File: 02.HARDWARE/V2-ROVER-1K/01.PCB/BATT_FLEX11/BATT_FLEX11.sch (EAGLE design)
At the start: 4 parts, among them K3 FLEX11, K4 FLEX11, K7 FLEX11, K8 FLEX11

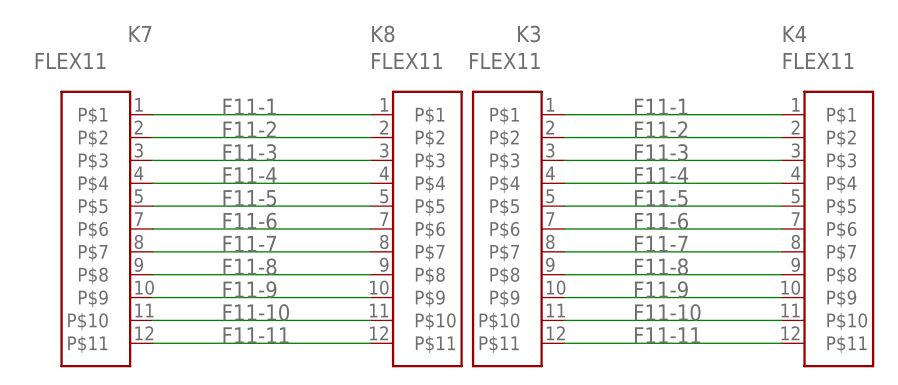
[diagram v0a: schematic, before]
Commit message: Ajuste de ancho de pista para lineas de potencias.
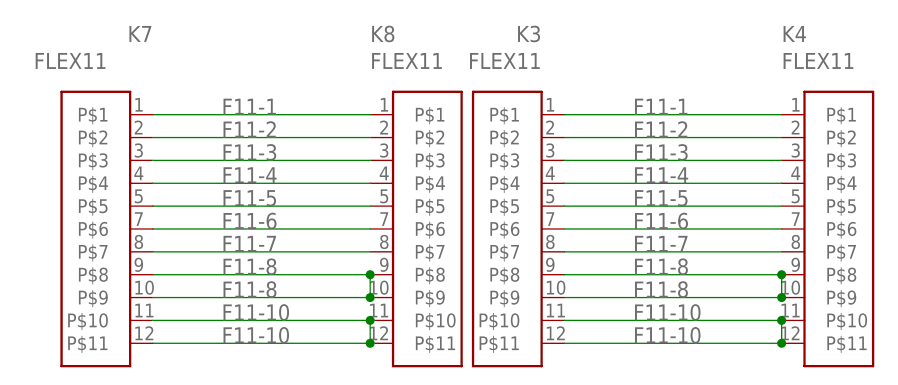
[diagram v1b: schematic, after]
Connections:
- removed net F11-11: K3.P$11, K4.P$11, K7.P$11, K8.P$11
- removed net F11-9: K3.P$9, K4.P$9, K7.P$9, K8.P$9
- net F11-10: now also K3.P$11, K4.P$11, K7.P$11, K8.P$11
- net F11-8: now also K3.P$9, K4.P$9, K7.P$9, K8.P$9
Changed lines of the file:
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@@
 <wire x1="124.46" y1="76.2" x2="148.59" y2="76.2" width="0.1524" layer="91"/>
 <label x="132.08" y="76.2" size="1.778" layer="95"/>
+<pinref part="K3" gate="G$1" pin="P$9"/>
+<pinref part="K4" gate="G$1" pin="P$9"/>
+<wire x1="124.46" y1="73.66" x2="148.59" y2="73.66" width="0.1524" layer="91"/>
+<label x="132.08" y="73.66" size="1.778" layer="95"/>
+<wire x1="148.59" y1="76.2" x2="148.59" y2="73.66" width="0.1524" layer="91"/>
+<junction x="148.59" y="76.2"/>
+<junction x="148.59" y="73.66"/>
 </segment>
 <segment>
@@
 <wire x1="78.74" y1="76.2" x2="102.87" y2="76.2" width="0.1524" layer="91"/>
 <label x="86.36" y="76.2" size="1.778" layer="95"/>
+<pinref part="K7" gate="G$1" pin="P$9"/>
+<pinref part="K8" gate="G$1" pin="P$9"/>
+<wire x1="78.74" y1="73.66" x2="102.87" y2="73.66" width="0.1524" layer="91"/>
+<label x="86.36" y="73.66" size="1.778" layer="95"/>
+<wire x1="102.87" y1="76.2" x2="102.87" y2="73.66" width="0.1524" layer="91"/>
+<junction x="102.87" y="76.2"/>
+<junction x="102.87" y="73.66"/>
 </segment>
 </net>
@@
 </segment>
 </net>
-<net name="F11-9" class="0">
-<segment>
-<pinref part="K7" gate="G$1" pin="P$9"/>
-<pinref part="K8" gate="G$1" pin="P$9"/>
-<wire x1="78.74" y1="73.66" x2="102.87" y2="73.66" width="0.1524" layer="91"/>
-<label x="86.36" y="73.66" size="1.778" layer="95"/>
-</segment>
-<segment>
-<pinref part="K3" gate="G$1" pin="P$9"/>
-<pinref part="K4" gate="G$1" pin="P$9"/>
-<wire x1="124.46" y1="73.66" x2="148.59" y2="73.66" width="0.1524" layer="91"/>
-<label x="132.08" y="73.66" size="1.778" layer="95"/>
-</segment>
-</net>
 <net name="F11-10" class="0">
 <segment>
@@
 <pinref part="K8" gate="G$1" pin="P$10"/>
 <label x="86.36" y="71.12" size="1.778" layer="95"/>
+<pinref part="K7" gate="G$1" pin="P$11"/>
+<pinref part="K8" gate="G$1" pin="P$11"/>
+<wire x1="78.74" y1="68.58" x2="102.87" y2="68.58" width="0.1524" layer="91"/>
+<label x="86.36" y="68.58" size="1.778" layer="95"/>
+<wire x1="102.87" y1="71.12" x2="102.87" y2="68.58" width="0.1524" layer="91"/>
+<junction x="102.87" y="71.12"/>
+<junction x="102.87" y="68.58"/>
 </segment>
 <segment>
@@
 <wire x1="148.59" y1="71.12" x2="124.46" y2="71.12" width="0.1524" layer="91"/>
 <label x="132.08" y="71.12" size="1.778" layer="95"/>
-</segment>
-</net>
-<net name="F11-11" class="0">
-<segment>
-<pinref part="K7" gate="G$1" pin="P$11"/>
-<pinref part="K8" gate="G$1" pin="P$11"/>
-<wire x1="78.74" y1="68.58" x2="102.87" y2="68.58" width="0.1524" layer="91"/>
-<label x="86.36" y="68.58" size="1.778" layer="95"/>
-</segment>
-<segment>
 <pinref part="K3" gate="G$1" pin="P$11"/>
 <pinref part="K4" gate="G$1" pin="P$11"/>
 <wire x1="124.46" y1="68.58" x2="148.59" y2="68.58" width="0.1524" layer="91"/>
 <label x="132.08" y="68.58" size="1.778" layer="95"/>
+<wire x1="148.59" y1="71.12" x2="148.59" y2="68.58" width="0.1524" layer="91"/>
+<junction x="148.59" y="71.12"/>
+<junction x="148.59" y="68.58"/>
 </segment>
 </net>
